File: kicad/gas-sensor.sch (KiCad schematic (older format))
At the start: 37 parts, among them J1 Conn FT232RL, J10 hole, J11 hole, J2 RJ12, J3 hole, J4 hole, J5 hole, J6 hole, J7 5V_Power_source, J8 hole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

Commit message: Update after debugging
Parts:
- added R6: 4,7k, Resistor_SMD:R_0805_2012Metric_Pad1.15x1.40mm_HandSolder, symbol Device:R
- added R7: R_Variable, symbol Device:R_Variable
- R2: value R -> 4,7
- R4: value 20k -> 22k
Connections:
- net +5V: now also GS3.6 (Vin), R6.1
- net GND: now also DS1.5 (R/W)
- net RX_MH-Z19: now also GS3.3 (TX), U2.25 (PC2); no longer GS3.2 (RX), U2.26 (PC3)
- net Sensor1_ON: now also U2.23 (PC0); no longer U2.19 (ADC6)
- net Sensor2: now also U2.19 (ADC6); no longer U2.23 (PC0)
- net TEMP: now also R6.2
- net TX_MH-Z19: now also GS3.2 (RX), U2.26 (PC3); no longer GS3.3 (TX), U2.25 (PC2)
- net VCC: now also R7.2; no longer DS1.3 (VO), GS3.6 (Vin)
- net LCD_RW: no longer names the net of U2.11 (PD7)
- net LCD_RW: no longer DS1.5 (R/W)
- new net: DS1.3 (VO), R7.1
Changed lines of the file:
@@
 $EndComp
 Text HLabel 9200 5600 0    50   Input ~ 0
-TX_MH-Z19
+RX_MH-Z19
 Wire Wire Line
 	9200 5600 9300 5600
 Text HLabel 9200 5750 0    50   Input ~ 0
-RX_MH-Z19
+TX_MH-Z19
 Wire Wire Line
 	9200 5750 9300 5750
@@
 	6750 4700 6500 4700
 Text HLabel 6750 3700 2    50   Input ~ 0
-TX_MH-Z19
+RX_MH-Z19
 Wire Wire Line
 	6750 4500 6500 4500
@@
 Wire Wire Line
 	5050 2600 5300 2600
-Text HLabel 5150 2800 0    50   Input ~ 0
+Text HLabel 6750 3500 2    50   Input ~ 0
 Sensor1_ON
 Wire Wire Line
@@
 	5150 2900 5300 2900
 Wire Wire Line
-	1550 850  1550 900
+	1550 750  1550 800
 Wire Wire Line
 	1550 1550 1550 1500
 Wire Wire Line
-	1950 1200 1850 1200
+	1950 1200 1900 1200
 Text HLabel 2950 950  0    50   Input ~ 0
 VCC-FTDI
@@
 Wire Wire Line
 	1000 6500 1350 6500
-$Comp
-L Display_Character:WC1602A DS1
-U 1 1 5C7BE6DA
-P 4050 6400
-F 0 "DS1" H 4550 6250 50  0000 C CNN
-F 1 "WC1602A" H 4550 6150 50  0000 C CNN
-F 2 "Display:WC1602A" H 4050 5500 50  0001 C CIN
-F 3 "http://www.wincomlcd.com/pdf/WC1602A-SFYLYHTC06.pdf" H 4750 6400 50  0001 C CNN
-	1    4050 6400
-	1    0    0    -1
-$EndComp
 Wire Wire Line
 	4050 5500 4050 5600
@@
 Wire Wire Line
 	4050 7300 4050 7200
-Text HLabel 6750 5000 2    50   Input ~ 0
-LCD_RW
-Wire Wire Line
-	6750 5000 6500 5000
 Text HLabel 3450 6700 0    50   Input ~ 0
 LCD1
@@
 Wire Wire Line
 	3450 6800 3650 6800
-Text HLabel 6750 3500 2    50   Input ~ 0
+Text HLabel 5150 2800 0    50   Input ~ 0
 Sensor2
 Wire Wire Line
@@
 $EndComp
 NoConn ~ 1350 6600
-$Comp
-L power:VCC #PWR028
-U 1 1 5C83C2AD
-P 10600 5900
-F 0 "#PWR028" H 10600 5750 50  0001 C CNN
-F 1 "VCC" H 10618 6073 50  0000 C CNN
-F 2 "" H 10600 5900 50  0001 C CNN
-F 3 "" H 10600 5900 50  0001 C CNN
-	1    10600 5900
-	-1   0    0    1
-$EndComp
 $Comp
 L Connector:Conn_01x06_Female J1
@@
 P 9300 2150
 F 0 "R4" H 9370 2196 50  0000 L CNN
-F 1 "20k" H 9370 2105 50  0000 L CNN
+F 1 "22k" H 9370 2105 50  0000 L CNN
 F 2 "Resistor_SMD:R_0805_2012Metric_Pad1.15x1.40mm_HandSolder" V 9230 2150 50  0001 C CNN
 F 3 "~" H 9300 2150 50  0001 C CNN
@@
 L power:+5V #PWR03
 U 1 1 5C81BEBA
-P 1550 850
-F 0 "#PWR03" H 1550 700 50  0001 C CNN
-F 1 "+5V" H 1565 1023 50  0000 C CNN
-F 2 "" H 1550 850 50  0001 C CNN
-F 3 "" H 1550 850 50  0001 C CNN
-	1    1550 850
+P 1550 750
+F 0 "#PWR03" H 1550 600 50  0001 C CNN
+F 1 "+5V" H 1565 923 50  0000 C CNN
+F 2 "" H 1550 750 50  0001 C CNN
+F 3 "" H 1550 750 50  0001 C CNN
+	1    1550 750
 	1    0    0    -1
 $EndComp
@@
 Wire Wire Line
 	3450 5800 3650 5800
-Text HLabel 3450 5900 0    50   Input ~ 0
-LCD_RW
-Wire Wire Line
-	3450 5900 3650 5900
 Text HLabel 3450 6000 0    50   Input ~ 0
 LCD_RS
 Wire Wire Line
 	3450 6000 3650 6000
-Wire Wire Line
-	4050 5500 4450 5500
-Wire Wire Line
-	4450 5500 4450 5800
-Connection ~ 4050 5500
 $Comp
 L Connector:Conn_Coaxial_Power J7
@@
 PWM_MH-Z19
 Text HLabel 6750 3800 2    50   Input ~ 0
-RX_MH-Z19
+TX_MH-Z19
 Text HLabel 6750 4500 2    50   Input ~ 0
 Sensor3
@@
 P 4700 6100
 F 0 "R2" V 4493 6100 50  0000 C CNN
-F 1 "R" V 4584 6100 50  0000 C CNN
+F 1 "4,7" V 4584 6100 50  0000 C CNN
 F 2 "Resistor_SMD:R_0805_2012Metric_Pad1.15x1.40mm_HandSolder" V 4630 6100 50  0001 C CNN
 F 3 "~" H 4700 6100 50  0001 C CNN
@@
 	1    0    0    -1
 $EndComp
+$Comp
+L power:GND #PWR0101
+U 1 1 5C964BAA
+P 2850 5900
+F 0 "#PWR0101" H 2850 5650 50  0001 C CNN
+F 1 "GND" H 2855 5727 50  0000 C CNN
+F 2 "" H 2850 5900 50  0001 C CNN
+F 3 "" H 2850 5900 50  0001 C CNN
+	1    2850 5900
+	1    0    0    -1
+$EndComp
+Wire Wire Line
+	2850 5900 3650 5900
+$Comp
+L Device:R R6
+U 1 1 5C96BDEE
+P 1900 950
+F 0 "R6" H 1970 996 50  0000 L CNN
+F 1 "4,7k" H 1970 905 50  0000 L CNN
+F 2 "Resistor_SMD:R_0805_2012Metric_Pad1.15x1.40mm_HandSolder" V 1830 950 50  0001 C CNN
+F 3 "~" H 1900 950 50  0001 C CNN
+	1    1900 950
+	1    0    0    -1
+$EndComp
+Wire Wire Line
+	1900 1100 1900 1200
+Connection ~ 1900 1200
+Wire Wire Line
+	1900 1200 1850 1200
+Wire Wire Line
+	1900 800  1550 800
+Wire Wire Line
+	1550 800  1550 900
+Connection ~ 1550 800
+$Comp
+L power:+5V #PWR0102
+U 1 1 5C99004F
+P 10600 5900
+F 0 "#PWR0102" H 10600 5750 50  0001 C CNN
+F 1 "+5V" H 10615 6073 50  0000 C CNN
+F 2 "" H 10600 5900 50  0001 C CNN
+F 3 "" H 10600 5900 50  0001 C CNN
+	1    10600 5900
+	1    0    0    -1
+$EndComp
+$Comp
+L Device:R_Variable R7
+U 1 1 5C99F42A
+P 4350 5600
+F 0 "R7" V 4105 5600 50  0000 C CNN
+F 1 "R_Variable" V 4196 5600 50  0000 C CNN
+F 2 "" V 4280 5600 50  0001 C CNN
+F 3 "~" H 4350 5600 50  0001 C CNN
+	1    4350 5600
+	0    1    1    0
+$EndComp
+$Comp
+L Display_Character:WC1602A DS1
+U 1 1 5C7BE6DA
+P 4050 6400
+F 0 "DS1" H 4550 6250 50  0000 C CNN
+F 1 "WC1602A" H 4550 6150 50  0000 C CNN
+F 2 "Display:WC1602A" H 4050 5500 50  0001 C CIN
+F 3 "http://www.wincomlcd.com/pdf/WC1602A-SFYLYHTC06.pdf" H 4750 6400 50  0001 C CNN
+	1    4050 6400
+	1    0    0    -1
+$EndComp
+Wire Wire Line
+	4200 5600 4050 5600
+Connection ~ 4050 5600
+Wire Wire Line
+	4500 5600 4500 5800
+Wire Wire Line
+	4500 5800 4450 5800
 $EndSCHEMATC

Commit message: Update
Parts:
- removed R7: R_Variable, symbol Device:R_Variable
- added R7: 3362P-103, symbol 3362P-103:3362P-103
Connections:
- net VCC: now also R7.1 (CCW)
- net at DS1.3 (VO): now also R7.3 (CW)
- no-connect marks 15 -> 17
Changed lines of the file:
@@
 $EndComp
 $Comp
-L Device:R_Variable R7
-U 1 1 5C99F42A
-P 4350 5600
-F 0 "R7" V 4105 5600 50  0000 C CNN
-F 1 "R_Variable" V 4196 5600 50  0000 C CNN
-F 2 "" V 4280 5600 50  0001 C CNN
-F 3 "~" H 4350 5600 50  0001 C CNN
-	1    4350 5600
-	0    1    1    0
+L 3362P-103:3362P-103 R7
+U 1 1 5C9C5387
+P 4750 5550
+F 0 "R7" H 4750 5865 50  0000 C CNN
+F 1 "3362P-103" H 4750 5774 50  0000 C CNN
+F 2 "" H 4750 5550 50  0001 C CNN
+F 3 "" H 4750 5550 50  0001 C CNN
+	1    4750 5550
+	1    0    0    -1
 $EndComp
+Connection ~ 4050 5500
 $Comp
 L Display_Character:WC1602A DS1
@@
 $EndComp
 Wire Wire Line
-	4200 5600 4050 5600
-Connection ~ 4050 5600
+	4050 5500 4350 5500
+NoConn ~ 4350 5600
 Wire Wire Line
-	4500 5600 4500 5800
+	5150 5500 5150 5800
 Wire Wire Line
-	4500 5800 4450 5800
+	4450 5800 5150 5800
+NoConn ~ 6500 5000
 $EndSCHEMATC

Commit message: Update
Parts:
- R7: footprint (none) -> TRIM_3362R-1-222:TRIM_3362R-1-222
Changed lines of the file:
@@
 F 0 "R7" H 4750 5865 50  0000 C CNN
 F 1 "3362P-103" H 4750 5774 50  0000 C CNN
-F 2 "" H 4750 5550 50  0001 C CNN
+F 2 "TRIM_3362R-1-222:TRIM_3362R-1-222" H 4750 5550 50  0001 C CNN
 F 3 "" H 4750 5550 50  0001 C CNN
 	1    4750 5550

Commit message: Rx/Tx + Potentiometer ok
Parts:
- R4: value 22k -> 4.7k
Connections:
- net RX: now also J1.4 (Pin_4); no longer J1.5 (Pin_5)
- net TX: now also J1.5 (Pin_5); no longer J1.4 (Pin_4)
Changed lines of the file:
@@
 $EndComp
 Text HLabel 1900 2650 2    50   Input ~ 0
-RX
+TX
 Wire Wire Line
 	1900 2650 1650 2650
 Text HLabel 1900 2750 2    50   Input ~ 0
-TX
+RX
 Wire Wire Line
 	1900 2750 1650 2750
@@
 P 9300 2150
 F 0 "R4" H 9370 2196 50  0000 L CNN
-F 1 "22k" H 9370 2105 50  0000 L CNN
+F 1 "4.7k" H 9370 2105 50  0000 L CNN
 F 2 "Resistor_SMD:R_0805_2012Metric_Pad1.15x1.40mm_HandSolder" V 9230 2150 50  0001 C CNN
 F 3 "~" H 9300 2150 50  0001 C CNN

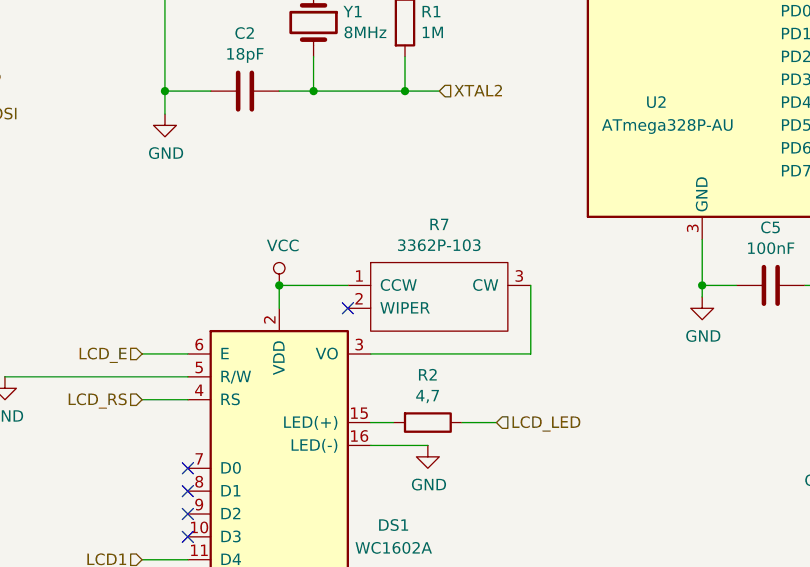
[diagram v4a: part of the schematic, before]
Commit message: Update
Plans for laser cut (simple & with clips)
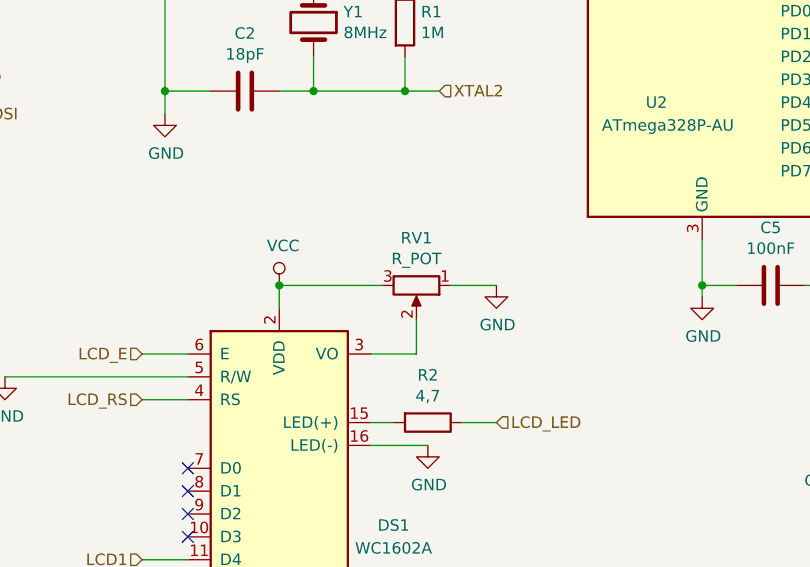
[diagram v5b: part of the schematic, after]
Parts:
- removed R7: 3362P-103, TRIM_3362R-1-222:TRIM_3362R-1-222, symbol 3362P-103:3362P-103
- added RV1: R_POT, TRIM_3362R-1-222:TRIM_3362R-1-222, symbol Device:R_POT
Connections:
- net GND: now also RV1.1
- net VCC: now also RV1.3
- net at DS1.3 (VO): now also RV1.2
- no-connect marks 17 -> 16
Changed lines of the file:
@@
-	1    0    0    -1
-$EndComp
-$Comp
-L 3362P-103:3362P-103 R7
-U 1 1 5C9C5387
-P 4750 5550
-F 0 "R7" H 4750 5865 50  0000 C CNN
-F 1 "3362P-103" H 4750 5774 50  0000 C CNN
-F 2 "TRIM_3362R-1-222:TRIM_3362R-1-222" H 4750 5550 50  0001 C CNN
-F 3 "" H 4750 5550 50  0001 C CNN
-	1    4750 5550
 	1    0    0    -1
 $EndComp
@@
 $EndComp
 Wire Wire Line
-	4050 5500 4350 5500
-NoConn ~ 4350 5600
+	4450 5800 4650 5800
+NoConn ~ 6500 5000
+$Comp
+L Device:R_POT RV1
+U 1 1 5CAD618B
+P 4650 5500
+F 0 "RV1" V 4443 5500 50  0000 C CNN
+F 1 "R_POT" V 4534 5500 50  0000 C CNN
+F 2 "TRIM_3362R-1-222:TRIM_3362R-1-222" H 4650 5500 50  0001 C CNN
+F 3 "~" H 4650 5500 50  0001 C CNN
+	1    4650 5500
+	0    1    1    0
+$EndComp
 Wire Wire Line
-	5150 5500 5150 5800
+	4050 5500 4500 5500
 Wire Wire Line
-	4450 5800 5150 5800
-NoConn ~ 6500 5000
+	4650 5650 4650 5800
+$Comp
+L power:GND #PWR0103
+U 1 1 5CAFAEC9
+P 5000 5500
+F 0 "#PWR0103" H 5000 5250 50  0001 C CNN
+F 1 "GND" H 5005 5327 50  0000 C CNN
+F 2 "" H 5000 5500 50  0001 C CNN
+F 3 "" H 5000 5500 50  0001 C CNN
+	1    5000 5500
+	1    0    0    -1
+$EndComp
+Wire Wire Line
+	5000 5500 4800 5500
 $EndSCHEMATC

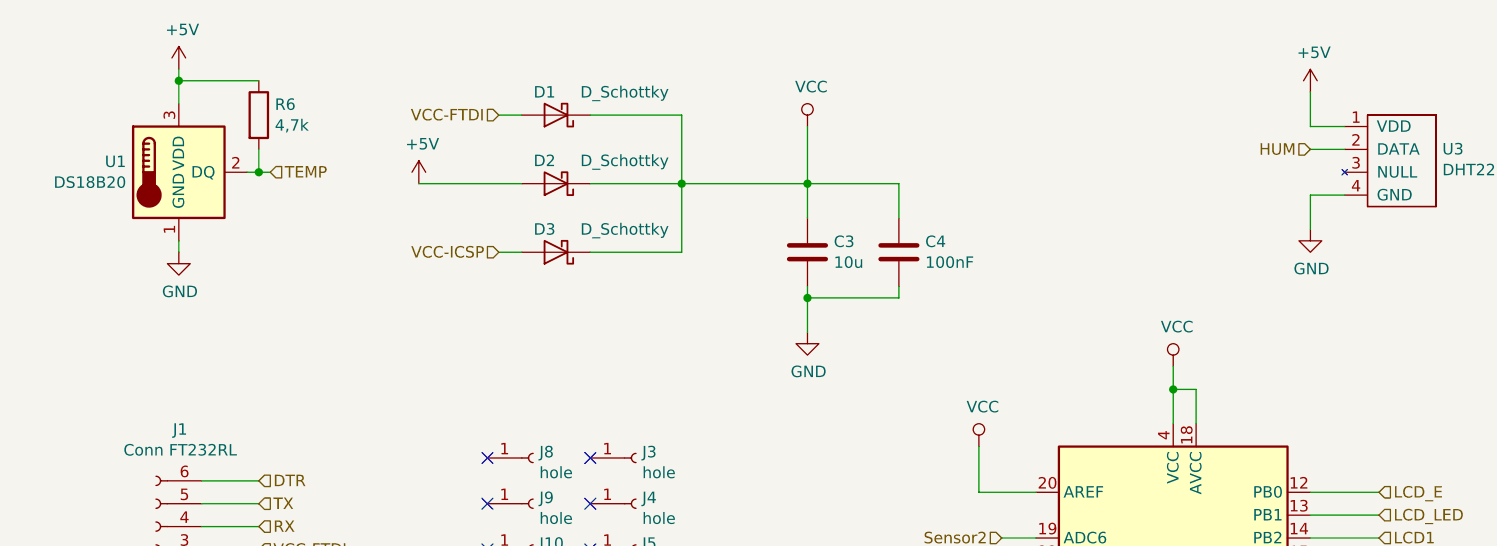
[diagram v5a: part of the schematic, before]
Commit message: Added voltage regulator
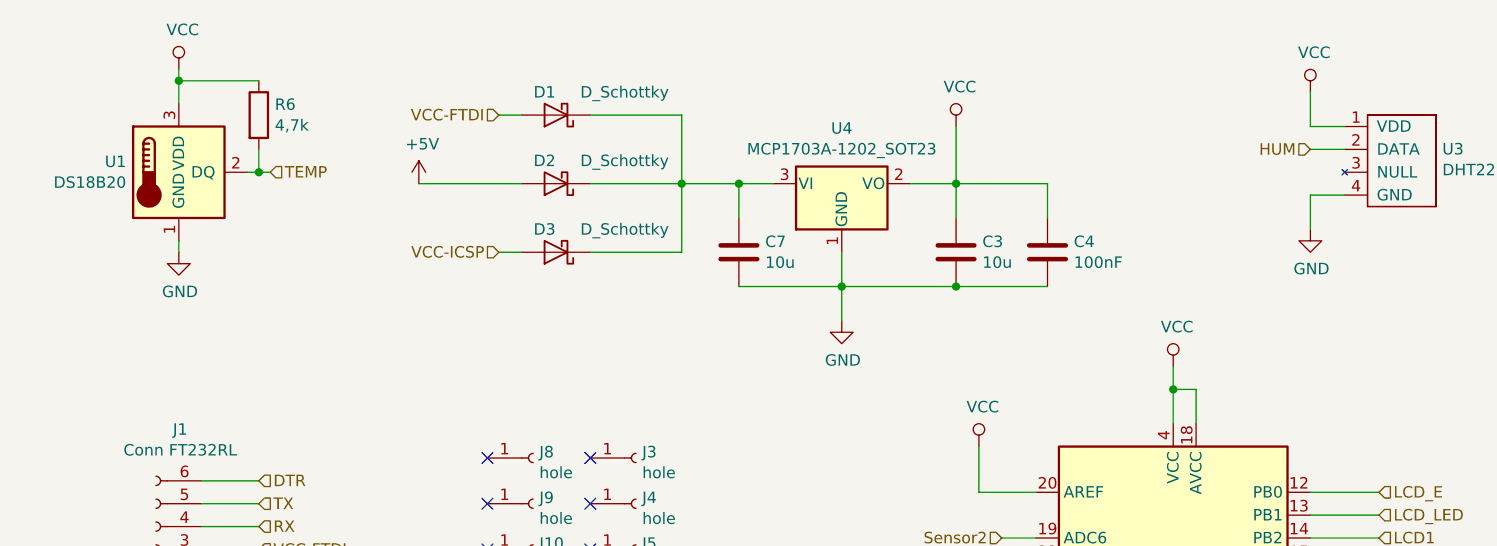
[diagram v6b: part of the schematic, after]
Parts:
- added C7: 10u, Capacitor_SMD:C_0805_2012Metric_Pad1.15x1.40mm_HandSolder, symbol Device:C
- added U4: MCP1703A-1202_SOT23, Package_TO_SOT_SMD:SOT-23, symbol Regulator_Linear:MCP1703A-1202_SOT23
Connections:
- net +5V: no longer R6.1, U1.3 (VDD), U3.1 (VDD)
- net GND: now also C7.2, U4.1 (GND)
- net VCC: now also R6.1, U1.3 (VDD), U3.1 (VDD), U4.2 (VO); no longer D1.1 (K), D2.1 (K), D3.1 (K)
- new net: C7.1, D1.1 (K), D2.1 (K), D3.1 (K), U4.3 (VI)
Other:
- moved on the sheet: C3, C4
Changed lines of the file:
@@
 L Device:C C3
 U 1 1 5C7867F7
-P 4300 1550
-F 0 "C3" H 4415 1596 50  0000 L CNN
-F 1 "10u" H 4415 1505 50  0000 L CNN
-F 2 "Capacitor_SMD:C_0805_2012Metric_Pad1.15x1.40mm_HandSolder" H 4338 1400 50  0001 C CNN
-F 3 "~" H 4300 1550 50  0001 C CNN
-	1    4300 1550
+P 4950 1550
+F 0 "C3" H 5065 1596 50  0000 L CNN
+F 1 "10u" H 5065 1505 50  0000 L CNN
+F 2 "Capacitor_SMD:C_0805_2012Metric_Pad1.15x1.40mm_HandSolder" H 4988 1400 50  0001 C CNN
+F 3 "~" H 4950 1550 50  0001 C CNN
+	1    4950 1550
 	1    0    0    -1
 $EndComp
@@
 L Device:C C4
 U 1 1 5C78684D
-P 4700 1550
-F 0 "C4" H 4815 1596 50  0000 L CNN
-F 1 "100nF" H 4815 1505 50  0000 L CNN
-F 2 "Capacitor_SMD:C_0805_2012Metric_Pad1.15x1.40mm_HandSolder" H 4738 1400 50  0001 C CNN
-F 3 "~" H 4700 1550 50  0001 C CNN
-	1    4700 1550
-	1    0    0    -1
-$EndComp
-Wire Wire Line
-	4700 1700 4700 1750
-Wire Wire Line
-	4300 1700 4300 1750
-Wire Wire Line
-	4300 1750 4700 1750
-Wire Wire Line
-	4700 1250 4700 1400
+P 5350 1550
+F 0 "C4" H 5465 1596 50  0000 L CNN
+F 1 "100nF" H 5465 1505 50  0000 L CNN
+F 2 "Capacitor_SMD:C_0805_2012Metric_Pad1.15x1.40mm_HandSolder" H 5388 1400 50  0001 C CNN
+F 3 "~" H 5350 1550 50  0001 C CNN
+	1    5350 1550
+	1    0    0    -1
+$EndComp
+Wire Wire Line
+	5350 1250 5350 1400
 Wire Wire Line
 	4600 4650 4200 4650
@@
 	1    0    0    -1
 $EndComp
-$Comp
-L power:+5V #PWR017
-U 1 1 5C7866DC
-P 6500 850
-F 0 "#PWR017" H 6500 700 50  0001 C CNN
-F 1 "+5V" H 6515 1023 50  0000 C CNN
-F 2 "" H 6500 850 50  0001 C CNN
-F 3 "" H 6500 850 50  0001 C CNN
-	1    6500 850
-	1    0    0    -1
-$EndComp
 Wire Wire Line
 	6500 850  6500 1000
@@
 NoConn ~ 1350 6200
 $Comp
-L power:GND #PWR012
-U 1 1 5C7F28E5
-P 4300 1900
-F 0 "#PWR012" H 4300 1650 50  0001 C CNN
-F 1 "GND" H 4305 1727 50  0000 C CNN
-F 2 "" H 4300 1900 50  0001 C CNN
-F 3 "" H 4300 1900 50  0001 C CNN
-	1    4300 1900
-	1    0    0    -1
-$EndComp
-Wire Wire Line
-	4300 1900 4300 1750
-Connection ~ 4300 1750
-$Comp
 L power:VCC #PWR011
 U 1 1 5C7FFF61
-P 4300 1000
-F 0 "#PWR011" H 4300 850 50  0001 C CNN
-F 1 "VCC" H 4317 1173 50  0000 C CNN
-F 2 "" H 4300 1000 50  0001 C CNN
-F 3 "" H 4300 1000 50  0001 C CNN
-	1    4300 1000
+P 4950 1000
+F 0 "#PWR011" H 4950 850 50  0001 C CNN
+F 1 "VCC" H 4967 1173 50  0000 C CNN
+F 2 "" H 4950 1000 50  0001 C CNN
+F 3 "" H 4950 1000 50  0001 C CNN
+	1    4950 1000
 	1    0    0    -1
 $EndComp
@@
 	1900 3050 1650 3050
 Wire Wire Line
-	4700 1250 4300 1250
-Wire Wire Line
-	4300 1000 4300 1250
-Connection ~ 4300 1250
-Wire Wire Line
-	4300 1250 3750 1250
-Wire Wire Line
-	4300 1400 4300 1250
+	5350 1250 4950 1250
+Wire Wire Line
+	4950 1000 4950 1250
+Connection ~ 4950 1250
+Wire Wire Line
+	4950 1400 4950 1250
 $Comp
 L BSP75:BSP75 Q1
@@
 Wire Wire Line
 	5900 5500 5900 5300
-$Comp
-L power:+5V #PWR03
-U 1 1 5C81BEBA
-P 1550 750
-F 0 "#PWR03" H 1550 600 50  0001 C CNN
-F 1 "+5V" H 1565 923 50  0000 C CNN
-F 2 "" H 1550 750 50  0001 C CNN
-F 3 "" H 1550 750 50  0001 C CNN
-	1    1550 750
-	1    0    0    -1
-$EndComp
 Wire Wire Line
 	6050 5500 5900 5500
@@
 Wire Wire Line
 	5000 5500 4800 5500
+$Comp
+L Regulator_Linear:MCP1703A-1202_SOT23 U4
+U 1 1 5CAE30C7
+P 4450 1250
+F 0 "U4" H 4450 1492 50  0000 C CNN
+F 1 "MCP1703A-1202_SOT23" H 4450 1401 50  0000 C CNN
+F 2 "Package_TO_SOT_SMD:SOT-23" H 4450 1450 50  0001 C CNN
+F 3 "http://ww1.microchip.com/downloads/en/DeviceDoc/20005122B.pdf" H 4450 1200 50  0001 C CNN
+	1    4450 1250
+	1    0    0    -1
+$EndComp
+Wire Wire Line
+	4950 1250 4750 1250
+Wire Wire Line
+	3750 1250 4000 1250
+$Comp
+L Device:C C7
+U 1 1 5CB5A06A
+P 4000 1550
+F 0 "C7" H 4115 1596 50  0000 L CNN
+F 1 "10u" H 4115 1505 50  0000 L CNN
+F 2 "Capacitor_SMD:C_0805_2012Metric_Pad1.15x1.40mm_HandSolder" H 4038 1400 50  0001 C CNN
+F 3 "~" H 4000 1550 50  0001 C CNN
+	1    4000 1550
+	1    0    0    -1
+$EndComp
+Wire Wire Line
+	4000 1400 4000 1250
+Connection ~ 4000 1250
+Wire Wire Line
+	4000 1250 4150 1250
+Wire Wire Line
+	4950 1700 5350 1700
+Connection ~ 4950 1700
+Wire Wire Line
+	4450 1550 4450 1700
+Connection ~ 4450 1700
+Wire Wire Line
+	4450 1700 4950 1700
+$Comp
+L power:GND #PWR0104
+U 1 1 5CB784C4
+P 4450 1850
+F 0 "#PWR0104" H 4450 1600 50  0001 C CNN
+F 1 "GND" H 4455 1677 50  0000 C CNN
+F 2 "" H 4450 1850 50  0001 C CNN
+F 3 "" H 4450 1850 50  0001 C CNN
+	1    4450 1850
+	1    0    0    -1
+$EndComp
+Wire Wire Line
+	4450 1850 4450 1700
+Wire Wire Line
+	4000 1700 4450 1700
+$Comp
+L power:VCC #PWR?
+U 1 1 5CB91526
+P 1550 750
+F 0 "#PWR?" H 1550 600 50  0001 C CNN
+F 1 "VCC" H 1567 923 50  0000 C CNN
+F 2 "" H 1550 750 50  0001 C CNN
+F 3 "" H 1550 750 50  0001 C CNN
+	1    1550 750
+	1    0    0    -1
+$EndComp
+$Comp
+L power:VCC #PWR?
+U 1 1 5CB998B1
+P 6500 850
+F 0 "#PWR?" H 6500 700 50  0001 C CNN
+F 1 "VCC" H 6517 1023 50  0000 C CNN
+F 2 "" H 6500 850 50  0001 C CNN
+F 3 "" H 6500 850 50  0001 C CNN
+	1    6500 850
+	1    0    0    -1
+$EndComp
 $EndSCHEMATC
